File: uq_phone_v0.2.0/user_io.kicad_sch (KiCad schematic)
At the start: 21 parts, among them J8 MCS-302S-C1, M1 C08-00A, Q3 S8050, U10 TPD8F003DQDR, U11 LSM6DSVTR, U12 DRV2603RUNR, U7 TPS22964CYZPR, U8 TPD3F303DQDR

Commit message: Add shared tray detect for MCU and RC7620 SIM detection
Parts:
- added Q6: MMBT3904LP-7, MMBT3904LP-7:DFN101X61X53-3N, symbol MMBT3904LP-7:MMBT3904LP-7
- added R37: 10k, Resistor_SMD:R_0201_0603Metric, symbol Resistors:Resistor_10k
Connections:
- net GND: now also Q6.2
- net uSD_TRAY_DET: now also R37.2
- new net: Q6.1, R37.1
- new net MOB_SIM_DET: Q6.3
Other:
- moved on the sheet: C29, C32, C33, DISP1, J8B, M1, Q3, R21, R26, R27, U12, U8

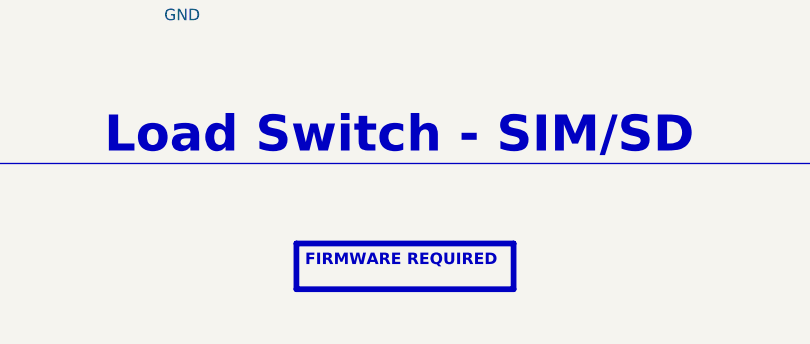
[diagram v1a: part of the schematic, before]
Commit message: Route soft power switch
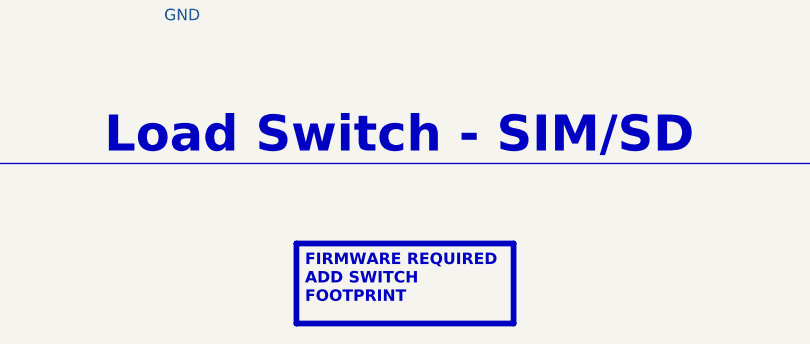
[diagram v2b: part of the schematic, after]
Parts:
- Q6: footprint MMBT3904LP-7:DFN101X61X53-3N -> MMBT3904LP-7:MMBT3904LP7
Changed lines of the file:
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@@
 		)
 	)
-	(text_box "FIRMWARE REQUIRED\n"
+	(text_box "FIRMWARE REQUIRED\nADD SWITCH FOOTPRINT\n"
 		(exclude_from_sim no)
 		(at 90.17 266.7 0)
-		(size 24.13 5.08)
+		(size 24.13 8.89)
 		(margins 0.9525 0.9525 0.9525 0.9525)
 		(stroke
@@
 			)
 		)
-		(property "Footprint" "MMBT3904LP-7:DFN101X61X53-3N"
+		(property "Footprint" "MMBT3904LP-7:MMBT3904LP7"
 			(at 217.17 59.69 0)
 			(effects

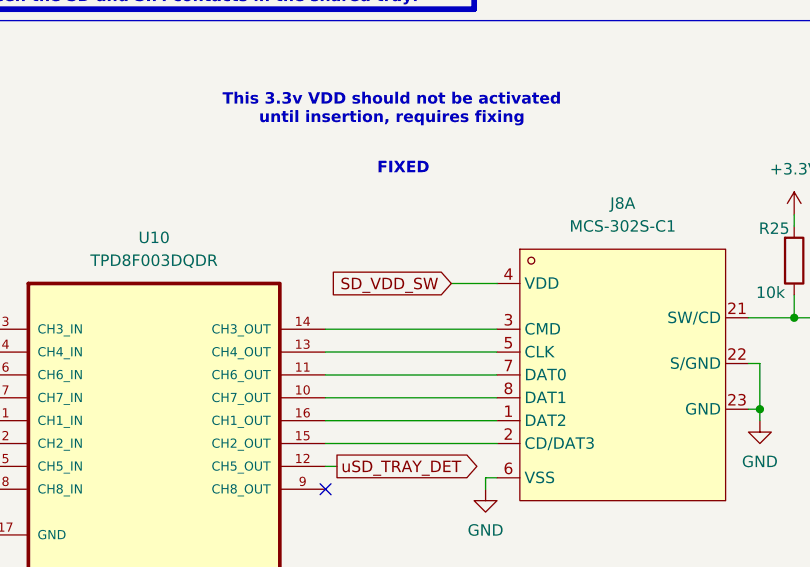
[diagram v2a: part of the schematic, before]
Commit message: Add headphone breakout board and update main PCB
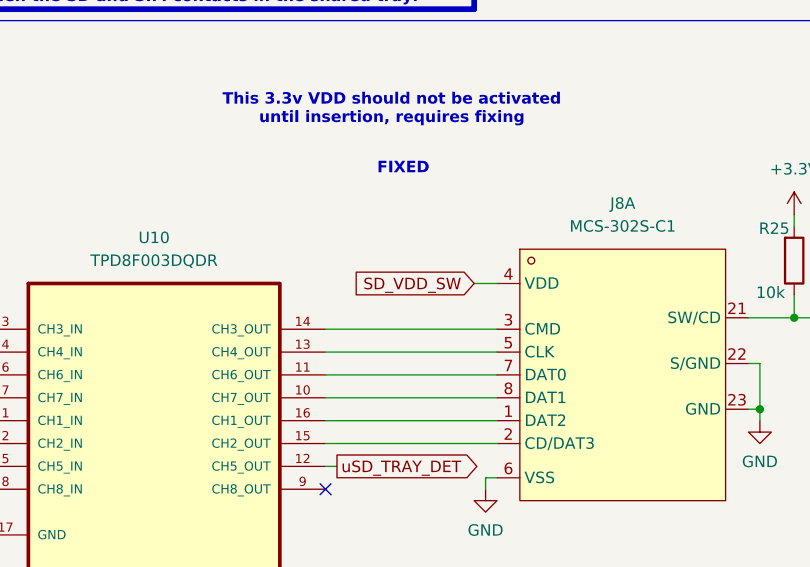
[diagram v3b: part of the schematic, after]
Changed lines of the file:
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@@
 	(wire
 		(pts
-			(xy 109.22 59.69) (xy 114.3 59.69)
+			(xy 111.76 59.69) (xy 114.3 59.69)
 		)
 		(stroke
@@
 	(global_label "SD_VDD_SW"
 		(shape input)
-		(at 109.22 59.69 180)
+		(at 111.76 59.69 180)
 		(fields_autoplaced yes)
 		(effects
@@
 		)
 		(property "Intersheetrefs" "${INTERSHEET_REFS}"
-			(at 95.5306 59.69 0)
+			(at 98.0706 59.69 0)
 			(effects
 				(font

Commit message: new display work
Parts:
- removed DISP1: HS20HS072RX, custom_footprints:Display, symbol Misc:HS20HS072RX
- removed Q3: S8050, Package_TO_SOT_SMD:SOT-23, symbol Misc:S8050
- removed R21: 10k, Resistor_SMD:R_0201_0603Metric, symbol Resistors:Resistor_10k
- removed R26: 1k, Resistor_SMD:R_0402_1005Metric, symbol Resistors:Resistor_1k
- removed R27: 5R, Resistor_SMD:R_0402_1005Metric, symbol Resistors:Resistor_5R
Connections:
- no-connect marks 14 -> 13

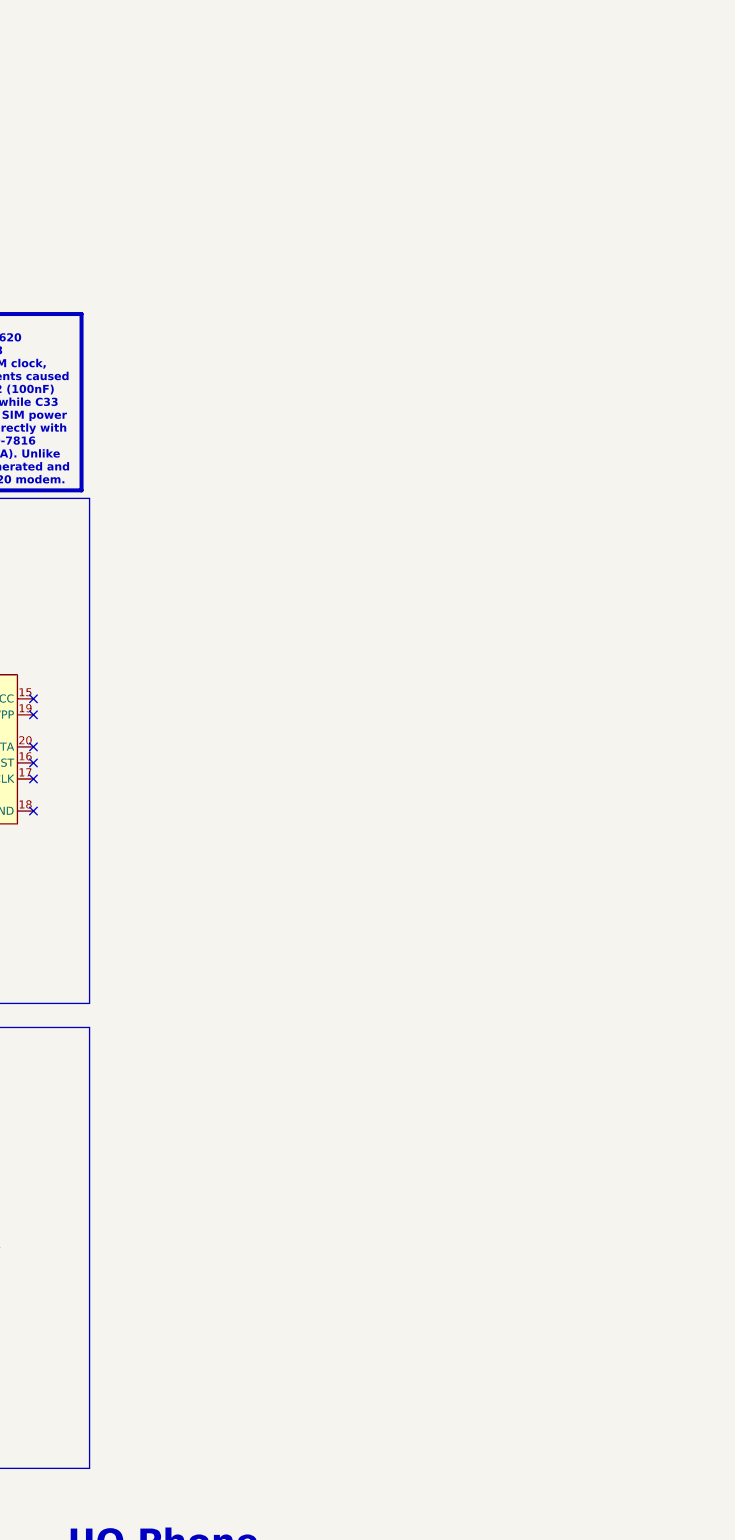
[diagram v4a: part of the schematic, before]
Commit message: Prototype without GPIO expander
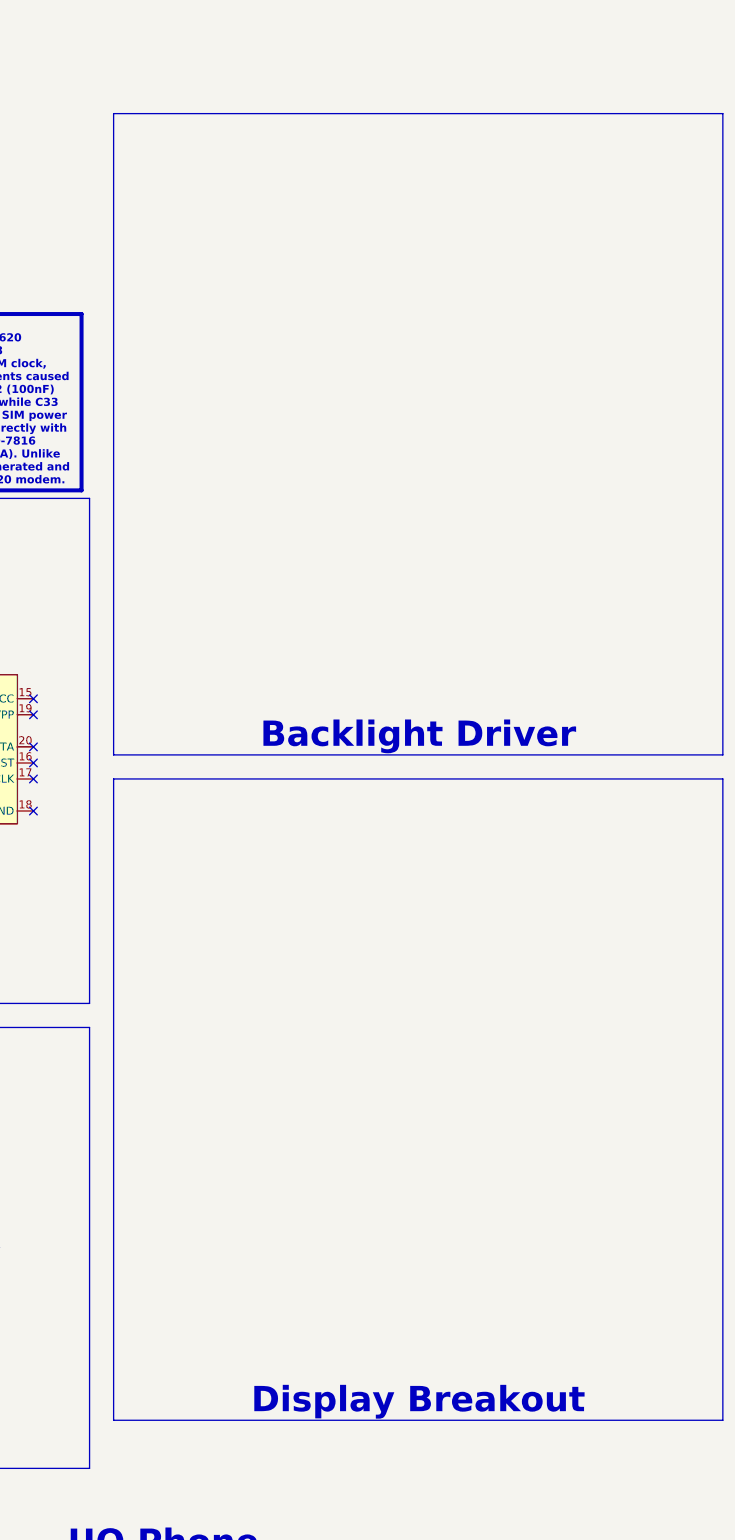
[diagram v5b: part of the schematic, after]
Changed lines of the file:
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@@
+		)
+	)
+	(text_box "Backlight Driver\n"
+		(exclude_from_sim no)
+		(at 308.61 31.75 0)
+		(size 96.52 101.6)
+		(margins 0.9525 0.9525 0.9525 0.9525)
+		(stroke
+			(width 0)
+			(type solid)
+		)
+		(fill
+			(type none)
+		)
+		(effects
+			(font
+				(size 4 4)
+				(thickness 1)
+				(bold yes)
+			)
+			(justify bottom)
 		)
 	)
@@
 		)
 	)
+	(text_box "Display Breakout\n"
+		(exclude_from_sim no)
+		(at 308.61 137.16 0)
+		(size 96.52 101.6)
+		(margins 0.9525 0.9525 0.9525 0.9525)
+		(stroke
+			(width 0)
+			(type solid)
+		)
+		(fill
+			(type none)
+		)
+		(effects
+			(font
+				(size 4 4)
+				(thickness 1)
+				(bold yes)
+			)
+			(justify bottom)
+		)
+	)

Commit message: Add GPIO expander and 16-bit FMC display schematic
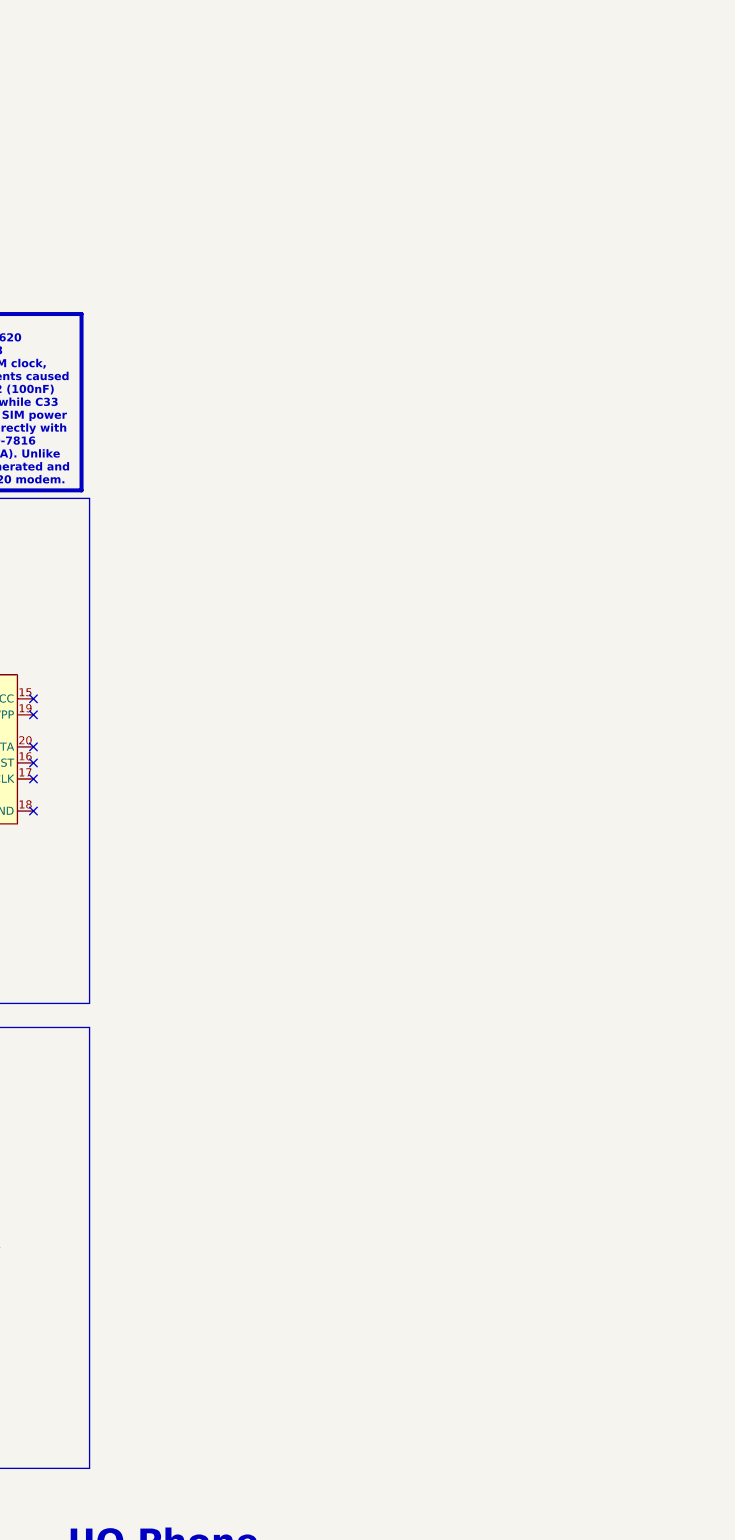
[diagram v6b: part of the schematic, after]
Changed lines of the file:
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@@
-		)
-	)
-	(text_box "Backlight Driver\n"
-		(exclude_from_sim no)
-		(at 308.61 31.75 0)
-		(size 96.52 101.6)
-		(margins 0.9525 0.9525 0.9525 0.9525)
-		(stroke
-			(width 0)
-			(type solid)
-		)
-		(fill
-			(type none)
-		)
-		(effects
-			(font
-				(size 4 4)
-				(thickness 1)
-				(bold yes)
-			)
-			(justify bottom)
 		)
 	)
@@
 		)
 	)
-	(text_box "Display Breakout\n"
-		(exclude_from_sim no)
-		(at 308.61 137.16 0)
-		(size 96.52 101.6)
-		(margins 0.9525 0.9525 0.9525 0.9525)
-		(stroke
-			(width 0)
-			(type solid)
-		)
-		(fill
-			(type none)
-		)
-		(effects
-			(font
-				(size 4 4)
-				(thickness 1)
-				(bold yes)
-			)
-			(justify bottom)
-		)
-	)
